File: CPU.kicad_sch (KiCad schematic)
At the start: 208 parts, among them J1 Conn_02x36_Odd_Even, P10 Conn_02x08_Counter_Clockwise, P2 Conn_02x13_Top_Bottom, P3 Conn_02x13_Top_Bottom, P4 Conn_02x08_Counter_Clockwise, P5 Conn_02x25_Counter_Clockwise, P6 Conn_02x25_Counter_Clockwise, P7 Conn_02x07_Counter_Clockwise, P8 Conn_02x08_Counter_Clockwise

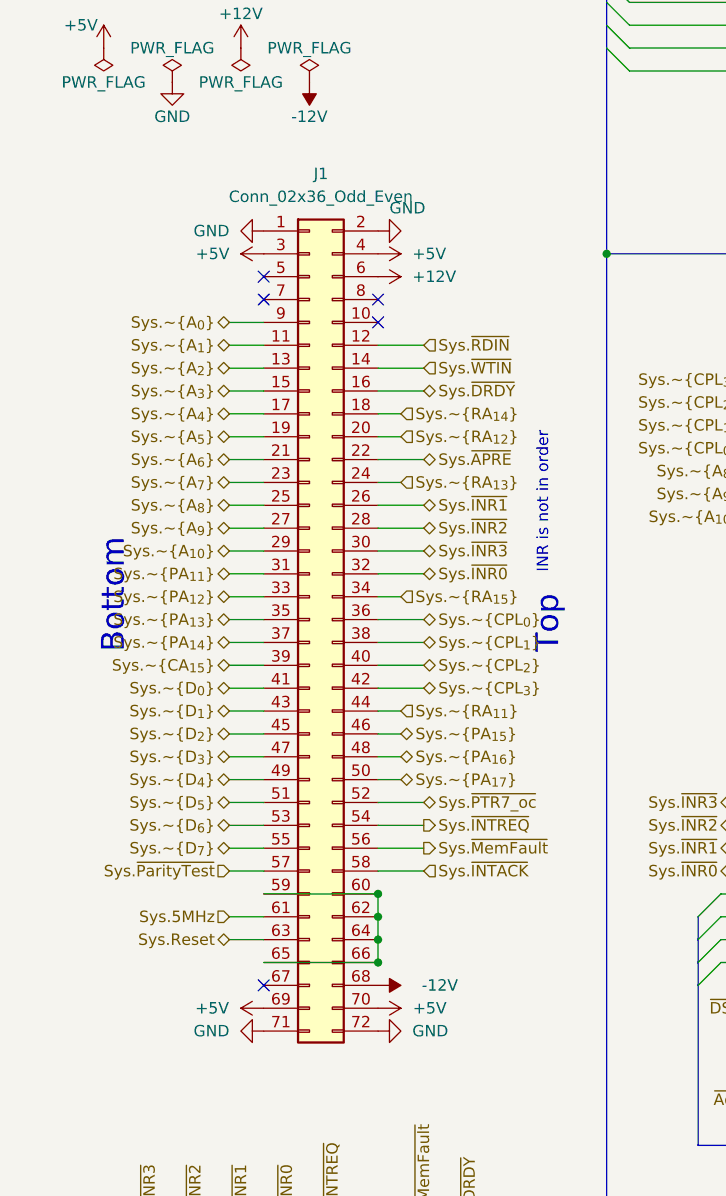
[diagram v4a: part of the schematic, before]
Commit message: Revert back to Centurion edge connector
Since i've found original connectors, there's no reason for substitution
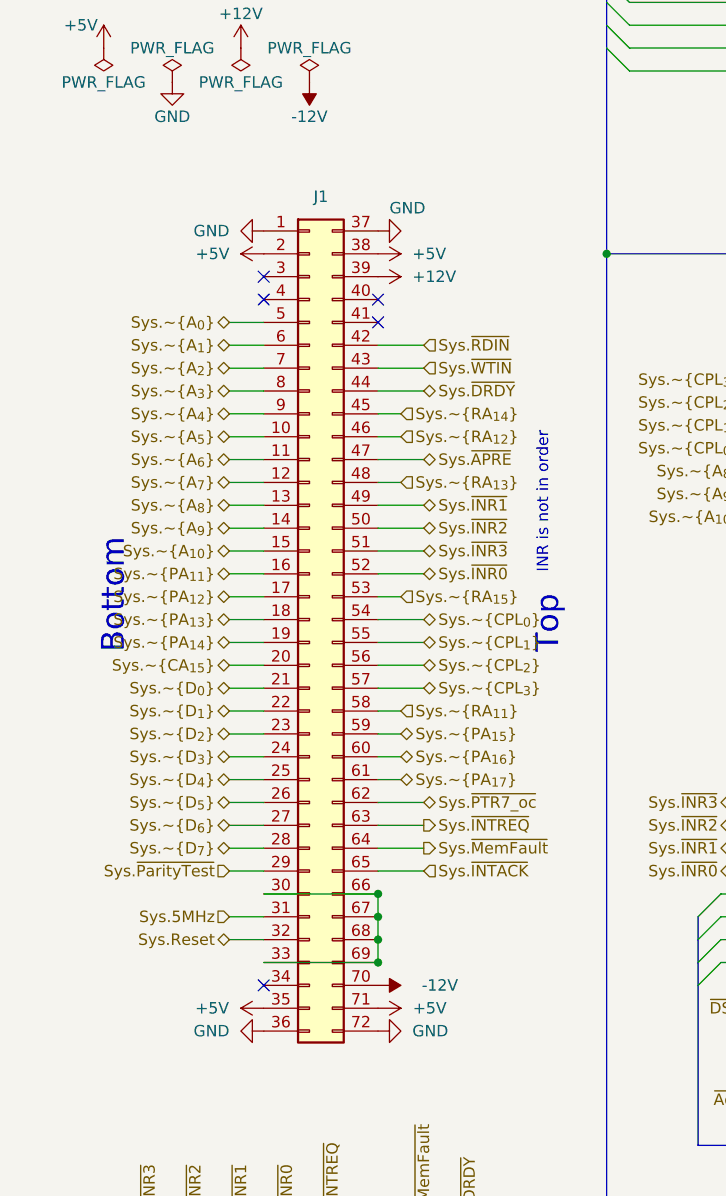
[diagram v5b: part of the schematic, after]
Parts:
- removed J1: Conn_02x36_Odd_Even, Connector_PinHeader_2.54mm:PinHeader_2x36_P2.54mm_Horizontal, symbol Connector_Generic:Conn_02x36_Odd_Even
- added J1: Conn_02x36_Top_Bottom, Connector_PCBEdge:BUS_EE200, symbol Connector_Generic:Conn_02x36_Top_Bottom
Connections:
- net +12V: now also J1.39 (Pin_39)
- net +5V: now also J1.2 (Pin_2), J1.35 (Pin_35), J1.38 (Pin_38), J1.71 (Pin_71)
- net -12V: now also J1.70 (Pin_70)
- net GND: now also J1.1 (Pin_1), J1.36 (Pin_36), J1.37 (Pin_37), J1.72 (Pin_72)
- net Sys.5MHz: now also J1.31 (Pin_31)
- net Sys.Reset: now also J1.32 (Pin_32)
- net Sys.~{APRE}: now also J1.47 (Pin_47)
- net Sys.~{A_{0}}: now also J1.5 (Pin_5)
- net Sys.~{A_{10}}: now also J1.15 (Pin_15)
- net Sys.~{A_{1}}: now also J1.6 (Pin_6)
- net Sys.~{A_{2}}: now also J1.7 (Pin_7)
- net Sys.~{A_{3}}: now also J1.8 (Pin_8)
- net Sys.~{A_{4}}: now also J1.9 (Pin_9)
- net Sys.~{A_{5}}: now also J1.10 (Pin_10)
- net Sys.~{A_{6}}: now also J1.11 (Pin_11)
- net Sys.~{A_{7}}: now also J1.12 (Pin_12)
- net Sys.~{A_{8}}: now also J1.13 (Pin_13)
- net Sys.~{A_{9}}: now also J1.14 (Pin_14)
- net Sys.~{CA_{15}}: now also J1.20 (Pin_20)
- net Sys.~{CPL_{0}}: now also J1.54 (Pin_54)
- net Sys.~{CPL_{1}}: now also J1.55 (Pin_55)
- net Sys.~{CPL_{2}}: now also J1.56 (Pin_56)
- net Sys.~{CPL_{3}}: now also J1.57 (Pin_57)
- net Sys.~{DRDY}: now also J1.44 (Pin_44)
- net Sys.~{D_{0}}: now also J1.21 (Pin_21)
- net Sys.~{D_{1}}: now also J1.22 (Pin_22)
- net Sys.~{D_{2}}: now also J1.23 (Pin_23)
- net Sys.~{D_{3}}: now also J1.24 (Pin_24)
- net Sys.~{D_{4}}: now also J1.25 (Pin_25)
- net Sys.~{D_{5}}: now also J1.26 (Pin_26)
- net Sys.~{D_{6}}: now also J1.27 (Pin_27)
- net Sys.~{D_{7}}: now also J1.28 (Pin_28)
- net Sys.~{INR0}: now also J1.52 (Pin_52)
- net Sys.~{INR1}: now also J1.49 (Pin_49)
- net Sys.~{INR2}: now also J1.50 (Pin_50)
- net Sys.~{INR3}: now also J1.51 (Pin_51)
- net Sys.~{INTACK}: now also J1.65 (Pin_65)
- net Sys.~{INTREQ}: now also J1.63 (Pin_63)
- net Sys.~{MemFault}: now also J1.64 (Pin_64)
- net Sys.~{PA_{11}}: now also J1.16 (Pin_16)
- net Sys.~{PA_{12}}: now also J1.17 (Pin_17)
- net Sys.~{PA_{13}}: now also J1.18 (Pin_18)
- net Sys.~{PA_{14}}: now also J1.19 (Pin_19)
- net Sys.~{PA_{15}}: now also J1.59 (Pin_59)
- net Sys.~{PA_{16}}: now also J1.60 (Pin_60)
- net Sys.~{PA_{17}}: now also J1.61 (Pin_61)
- net Sys.~{PTR7_oc}: now also J1.62 (Pin_62)
- net Sys.~{ParityTest}: now also J1.29 (Pin_29)
- net Sys.~{RA_{11}}: now also J1.58 (Pin_58)
- net Sys.~{RA_{12}}: now also J1.46 (Pin_46)
- net Sys.~{RA_{13}}: now also J1.48 (Pin_48)
- net Sys.~{RA_{14}}: now also J1.45 (Pin_45)
- net Sys.~{RA_{15}}: now also J1.53 (Pin_53)
- net Sys.~{RDIN}: now also J1.42 (Pin_42)
- net Sys.~{WTIN}: now also J1.43 (Pin_43)
- new net: J1.30 (Pin_30), J1.33 (Pin_33), J1.66 (Pin_66), J1.67 (Pin_67), J1.68 (Pin_68), J1.69 (Pin_69)
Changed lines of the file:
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@@
   (junction (at 1065.53 707.39) (diameter 0) (color 0 0 0 0)
   )
-  (junction (at 58.42 449.58) (diameter 0) (color 0 0 0 0)
-  )
   (junction (at 661.67 29.21) (diameter 0) (color 0 0 0 0)
   )
@@
   (junction (at 335.28 76.2) (diameter 0) (color 0 0 0 0)
   )
+  (junction (at 58.42 449.58) (diameter 0) (color 0 0 0 0)
+  )
   (junction (at 452.12 292.1) (diameter 0) (color 0 0 0 0)
   )
@@
   (junction (at 1078.23 680.72) (diameter 0) (color 0 0 0 0)
   )
+  (junction (at 58.42 452.12) (diameter 0) (color 0 0 0 0)
+  )
   (junction (at 753.11 768.35) (diameter 0) (color 0 0 0 0)
   )
@@
   (junction (at 245.11 364.49) (diameter 0) (color 0 0 0 0)
   )
+  (junction (at 58.42 457.2) (diameter 0) (color 0 0 0 0)
+  )
   (junction (at 605.79 763.27) (diameter 0) (color 0 0 0 0)
   )
@@
   (junction (at 146.05 330.2) (diameter 0) (color 0 0 0 0)
   )
-  (junction (at 58.42 452.12) (diameter 0) (color 0 0 0 0)
-  )
   (junction (at 494.03 308.61) (diameter 0) (color 0 0 0 0)
   )
@@
   (junction (at 763.27 814.07) (diameter 0) (color 0 0 0 0)
   )
-  (junction (at 58.42 457.2) (diameter 0) (color 0 0 0 0)
-  )
   (junction (at 1158.24 657.86) (diameter 0) (color 0 0 0 0)
   )
@@
   (junction (at 778.51 814.07) (diameter 0) (color 0 0 0 0)
   )
-  (junction (at 58.42 454.66) (diameter 0) (color 0 0 0 0)
-  )
   (junction (at 661.67 760.73) (diameter 0) (color 0 0 0 0)
   )
@@
   (junction (at 351.79 693.42) (diameter 0) (color 0 0 0 0)
   )
+  (junction (at 58.42 454.66) (diameter 0) (color 0 0 0 0)
+  )
   (junction (at 1101.09 692.15) (diameter 0) (color 0 0 0 0)
   )
@@
     (stroke (width 0) (type default) (color 0 0 0 0))
   )
+  (wire (pts (xy 58.42 454.66) (xy 58.42 457.2))
+    (stroke (width 0) (type default) (color 0 0 0 0))
+  )
   (wire (pts (xy 86.36 600.71) (xy 111.76 600.71))
     (stroke (width 0) (type default) (color 0 0 0 0))
@@
     (stroke (width 0) (type default) (color 0 0 0 0))
   )
-  (wire (pts (xy 58.42 449.58) (xy 58.42 452.12))
-    (stroke (width 0) (type default) (color 0 0 0 0))
-  )
   (wire (pts (xy 196.85 63.5) (xy 212.09 63.5))
     (stroke (width 0) (type default) (color 0 0 0 0))
@@
     (stroke (width 0) (type default) (color 0 0 0 0))
   )
-  (wire (pts (xy 58.42 454.66) (xy 58.42 457.2))
-    (stroke (width 0) (type default) (color 0 0 0 0))
-  )
   (wire (pts (xy 201.93 50.8) (xy 212.09 50.8))
     (stroke (width 0) (type default) (color 0 0 0 0))
@@
     (stroke (width 0) (type default) (color 189 121 184 1))
   )
-  (wire (pts (xy 58.42 452.12) (xy 58.42 454.66))
+  (wire (pts (xy 58.42 449.58) (xy 58.42 452.12))
     (stroke (width 0) (type default) (color 0 0 0 0))
   )
@@
     (stroke (width 0) (type default) (color 243 83 82 1))
   )
+  (wire (pts (xy 58.42 452.12) (xy 58.42 454.66))
+    (stroke (width 0) (type default) (color 0 0 0 0))
+  )
   (wire (pts (xy 328.93 378.46) (xy 356.87 378.46))
     (stroke (width 0) (type default) (color 0 0 0 0))
@@
     (pin "1")
   )
-  (symbol (lib_id "Connector_Generic:Conn_02x36_Odd_Even") (at 50.8 419.1 0) (unit 1)
-    (in_bom yes) (on_board yes) (fields_autoplaced)
-    (property "Reference" "J1" (id 0) (at 52.07 369.57 0))
-    (property "Value" "Conn_02x36_Odd_Even" (id 1) (at 52.07 372.11 0))
-    (property "Footprint" "Connector_PinHeader_2.54mm:PinHeader_2x36_P2.54mm_Horizontal" (id 2) (at 50.8 419.1 0)
-      (effects (font (size 1.27 1.27)) hide)
-    )
-    (property "Datasheet" "~" (id 3) (at 50.8 419.1 0)
-      (effects (font (size 1.27 1.27)) hide)
-    )
-    (pin "1")
-    (pin "10")
-    (pin "11")
-    (pin "12")
-    (pin "13")
-    (pin "14")
-    (pin "15")
-    (pin "16")
-    (pin "17")
-    (pin "18")
-    (pin "19")
-    (pin "2")
-    (pin "20")
-    (pin "21")
-    (pin "22")
-    (pin "23")
-    (pin "24")
-    (pin "25")
-    (pin "26")
-    (pin "27")
-    (pin "28")
-    (pin "29")
-    (pin "3")
-    (pin "30")
-    (pin "31")
-    (pin "32")
-    (pin "33")
-    (pin "34")
-    (pin "35")
-    (pin "36")
-    (pin "37")
-    (pin "38")
-    (pin "39")
-    (pin "4")
-    (pin "40")
-    (pin "41")
-    (pin "42")
-    (pin "43")
-    (pin "44")
-    (pin "45")
-    (pin "46")
-    (pin "47")
-    (pin "48")
-    (pin "49")
-    (pin "5")
-    (pin "50")
-    (pin "51")
-    (pin "52")
-    (pin "53")
-    (pin "54")
-    (pin "55")
-    (pin "56")
-    (pin "57")
-    (pin "58")
-    (pin "59")
-    (pin "6")
-    (pin "60")
-    (pin "61")
-    (pin "62")
-    (pin "63")
-    (pin "64")
-    (pin "65")
-    (pin "66")
-    (pin "67")
-    (pin "68")
-    (pin "69")
-    (pin "7")
-    (pin "70")
-    (pin "71")
-    (pin "72")
-    (pin "8")
-    (pin "9")
-  )
   (symbol (lib_id "Device:C_Small") (at 1032.51 683.26 0) (unit 1)
     (in_bom yes) (on_board yes)
@@
     (pin "2")
   )
+  (symbol (lib_id "Connector_Generic:Conn_02x36_Top_Bottom") (at 50.8 419.1 0) (unit 1)
+    (in_bom yes) (on_board yes) (fields_autoplaced)
+    (property "Reference" "J1" (id 0) (at 52.07 372.11 0))
+    (property "Value" "Conn_02x36_Top_Bottom" (id 1) (at 52.07 372.11 0)
+      (effects (font (size 1.27 1.27)) hide)
+    )
+    (property "Footprint" "Connector_PCBEdge:BUS_EE200" (id 2) (at 50.8 419.1 0)
+      (effects (font (size 1.27 1.27)) hide)
+    )
+    (property "Datasheet" "~" (id 3) (at 50.8 419.1 0)
+      (effects (font (size 1.27 1.27)) hide)
+    )
+    (pin "1")
+    (pin "10")
+    (pin "11")
+    (pin "12")
+    (pin "13")
+    (pin "14")
+    (pin "15")
+    (pin "16")
+    (pin "17")
+    (pin "18")
+    (pin "19")
+    (pin "2")
+    (pin "20")
+    (pin "21")
+    (pin "22")
+    (pin "23")
+    (pin "24")
+    (pin "25")
+    (pin "26")
+    (pin "27")
+    (pin "28")
+    (pin "29")
+    (pin "3")
+    (pin "30")
+    (pin "31")
+    (pin "32")
+    (pin "33")
+    (pin "34")
+    (pin "35")
+    (pin "36")
+    (pin "37")
+    (pin "38")
+    (pin "39")
+    (pin "4")
+    (pin "40")
+    (pin "41")
+    (pin "42")
+    (pin "43")
+    (pin "44")
+    (pin "45")
+    (pin "46")
+    (pin "47")
+    (pin "48")
+    (pin "49")
+    (pin "5")
+    (pin "50")
+    (pin "51")
+    (pin "52")
+    (pin "53")
+    (pin "54")
+    (pin "55")
+    (pin "56")
+    (pin "57")
+    (pin "58")
+    (pin "59")
+    (pin "6")
+    (pin "60")
+    (pin "61")
+    (pin "62")
+    (pin "63")
+    (pin "64")
+    (pin "65")
+    (pin "66")
+    (pin "67")
+    (pin "68")
+    (pin "69")
+    (pin "7")
+    (pin "70")
+    (pin "71")
+    (pin "72")
+    (pin "8")
+    (pin "9")
+  )
   (symbol (lib_id "power:GND") (at 674.37 579.12 0) (unit 1)
     (in_bom yes) (on_board yes)
@@
       (reference "DSW1") (unit 1) (value "SW_DIP_x08") (footprint "Button_Switch_THT:SW_DIP_SPSTx08_Piano_10.8x21.88mm_W7.62mm_P2.54mm")
     )
-    (path "/204a5142-3c33-4dca-b85e-682e0b14a381"
-      (reference "J1") (unit 1) (value "Conn_02x36_Odd_Even") (footprint "Connector_PinHeader_2.54mm:PinHeader_2x36_P2.54mm_Horizontal")
+    (path "/cf5ff769-b920-409b-9085-8668ccbbaa16"
+      (reference "J1") (unit 1) (value "Conn_02x36_Top_Bottom") (footprint "Connector_PCBEdge:BUS_EE200")
     )
     (path "/25a6a420-d138-460a-9a95-c8a71db3148b"

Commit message: Optimized nets around A6, A7, A8
Pins reordered to reduce criss-crossing
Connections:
- net Address.A_{12}: now also U_A3.11; no longer U_A3.9
- net Address.A_{14}: now also U_A3.9; no longer U_A3.11
- net Address.A_{8}: no longer U_A6.11 (I0b)
- net CPL_{0}: now also U_A6.2 (I0a), U_A8.2 (I0a); no longer U_A6.8 (I3a), U_A8.8 (I3a)
- net CPL_{1}: now also U_A6.4 (I1a), U_A8.4 (I1a); no longer U_A6.6 (I2a), U_A8.6 (I2a)
- net CPL_{2}: now also U_A6.6 (I2a), U_A8.6 (I2a); no longer U_A6.4 (I1a), U_A8.4 (I1a)
- net CPL_{3}: now also U_A6.8 (I3a), U_A8.8 (I3a); no longer U_A6.2 (I0a), U_A8.2 (I0a)
- net DataP.D_{4}: now also U_A6.18 (O0a), U_A7.18 (O0a); no longer U_A6.12 (O3a), U_A7.12 (O3a)
- net DataP.D_{5}: now also U_A6.16 (O1a), U_A7.16 (O1a); no longer U_A6.14 (O2a), U_A7.14 (O2a)
- net DataP.D_{6}: now also U_A6.14 (O2a), U_A7.14 (O2a), U_A9.14 (O2a); no longer U_A6.16 (O1a), U_A7.16 (O1a), U_A9.12 (O3a)
- net DataP.D_{7}: now also U_A6.12 (O3a), U_A7.12 (O3a), U_A9.12 (O3a); no longer U_A6.18 (O0a), U_A7.18 (O0a), U_A9.14 (O2a)
- net PTR.Q_{6}: now also U_A9.6 (I2a); no longer U_A9.8 (I3a)
- net Sys.~{CPL_{0}}: now also U_A8.18 (O0a); no longer U_A8.12 (O3a)
- net Sys.~{CPL_{1}}: now also U_A8.16 (O1a); no longer U_A8.14 (O2a)
- net Sys.~{CPL_{2}}: now also U_A8.14 (O2a); no longer U_A8.16 (O1a)
- net Sys.~{CPL_{3}}: now also U_A8.12 (O3a); no longer U_A8.18 (O0a)
- net Sys.~{INR0}: now also U_A7.2 (I0a); no longer U_A7.8 (I3a)
- net Sys.~{INR1}: now also U_A7.4 (I1a); no longer U_A7.6 (I2a)
- net Sys.~{INR2}: now also U_A7.6 (I2a); no longer U_A7.4 (I1a)
- net Sys.~{INR3}: now also U_A7.8 (I3a); no longer U_A7.2 (I0a)
- net Sys.~{RA_{12}}: now also U_A3.10; no longer U_A3.8
- net Sys.~{RA_{14}}: now also U_A3.8; no longer U_A3.10
- net at U_A10.6 (I2a), U_C8.12: now also U_A9.8 (I3a); no longer U_A9.6 (I2a)

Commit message: Substitute RN16
A dual 330+220 ohm resistor network appears to only be available in DIP package
here; additionally having these resistors in one assembly requires more long
traces, which are very inconvenient in connector area as both layers are quite
busy. Break it down into individual parts.
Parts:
- removed RN16: 220/330, Resistor_THT:R_Array_SIP10, symbol Device:R_Network_Dividers_x08_SIP
- added R22, R24, R26: 220, Resistor_THT:R_Axial_DIN0204_L3.6mm_D1.6mm_P2.54mm_Vertical, symbol Device:R
- added R23, R25, R27: 330, Resistor_THT:R_Axial_DIN0204_L3.6mm_D1.6mm_P2.54mm_Vertical, symbol Device:R
- added RN20: 220, Resistor_THT:R_Array_SIP5, symbol Device:R_Network04
- added RN21: 330, Resistor_THT:R_Array_SIP5, symbol Device:R_Network04
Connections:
- net +5V: now also R22.1, R24.1, R26.1, RN20.1 (common)
- net GND: now also R23.2, R25.2, R27.2, RN21.1 (common)
- net Sys.~{DRDY}: now also R22.2, R23.1
- net Sys.~{INR0}: now also RN20.5 (R4), RN21.5 (R4)
- net Sys.~{INR1}: now also RN20.2 (R1), RN21.2 (R1)
- net Sys.~{INR2}: now also RN20.3 (R2), RN21.3 (R2)
- net Sys.~{INR3}: now also RN20.4 (R3), RN21.4 (R3)
- net Sys.~{INTREQ}: now also R26.2, R27.1
- net Sys.~{MemFault}: now also R24.2, R25.1
- no-connect marks 95 -> 94
